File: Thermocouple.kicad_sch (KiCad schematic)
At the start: 9 parts, among them J7 K-TYPE THERMOCOUPLE, U11 MAX31856

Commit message: 9/13/2026 schematic work
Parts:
- C16, C17, C18: value 0.1uF -> 0.1u
- C19, C28: value 0.01uF -> 0.01u
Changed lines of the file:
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@@
 		(dnp no)
 		(property "Reference" "C18"
-			(at 142.748 77.216 0)
-			(show_name no)
-			(do_not_autoplace no)
-			(effects
-				(font
-					(size 1.27 1.27)
-				)
-				(justify left)
-			)
-		)
-		(property "Value" "0.1uF"
-			(at 147.066 77.47 0)
+			(at 146.558 71.628 90)
+			(show_name no)
+			(do_not_autoplace no)
+			(effects
+				(font
+					(size 1.27 1.27)
+				)
+				(justify left)
+			)
+		)
+		(property "Value" "0.1u"
+			(at 146.812 73.66 90)
 			(show_name no)
 			(do_not_autoplace no)
@@
 		(in_pos_files yes)
 		(dnp no)
-		(fields_autoplaced yes)
 		(property "Reference" "U11"
-			(at 169.7833 71.12 0)
+			(at 171.196 74.93 0)
 			(show_name no)
 			(do_not_autoplace no)
@@
 		)
 		(property "Value" "MAX31856"
-			(at 169.7833 73.66 0)
+			(at 168.656 102.87 0)
 			(show_name no)
 			(do_not_autoplace no)
@@
 			)
 		)
-		(property "Value" "0.1uF"
+		(property "Value" "0.1u"
 			(at 168.402 68.326 0)
 			(show_name no)
@@
 			)
 		)
-		(property "Value" "0.1uF"
+		(property "Value" "0.1u"
 			(at 156.21 68.326 0)
 			(show_name no)
@@
 			)
 		)
-		(property "Value" "0.01uF"
-			(at 127 98.806 0)
+		(property "Value" "0.01u"
+			(at 127.508 98.806 0)
 			(show_name no)
 			(do_not_autoplace no)
@@
 			)
 		)
-		(property "Value" "0.01uF"
-			(at 135.89 98.806 0)
-			(show_name no)
-			(do_not_autoplace no)
+		(property "Value" "0.01u"
+			(at 136.652 98.806 0)
+			(show_name no)
+			(do_not_autoplace no)

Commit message: changed sheet names
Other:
- title: Thermocouple Input -> Thermocouple
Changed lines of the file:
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@@
 	(paper "A")
 	(title_block
-		(title "Thermocouple Input")
+		(title "Thermocouple")
 		(date "2026-09-08")
 		(rev "1")

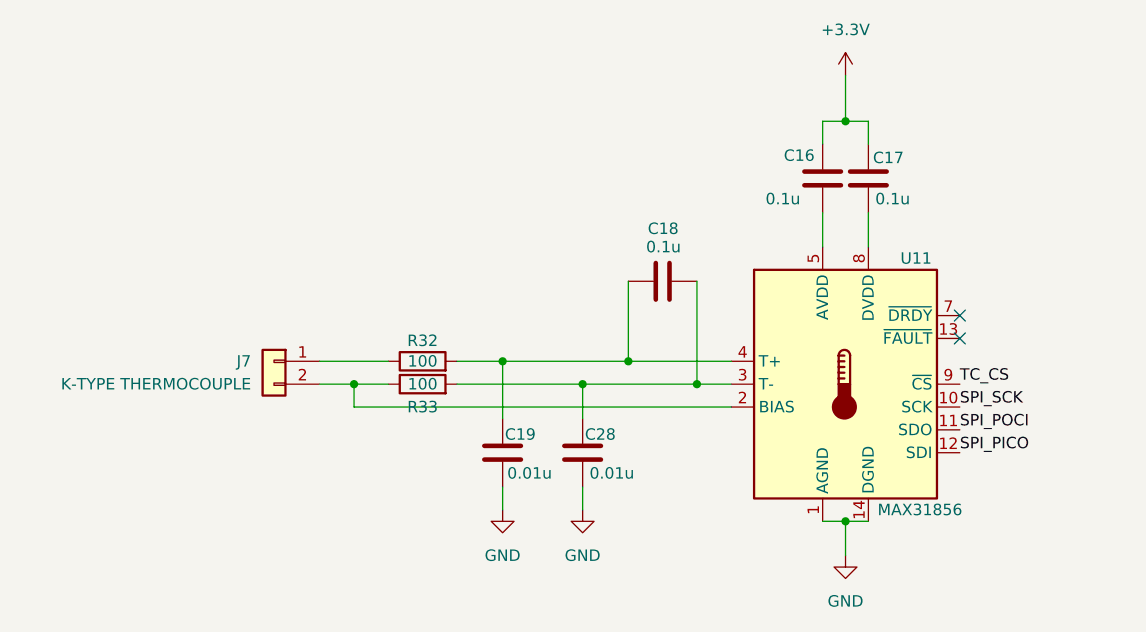
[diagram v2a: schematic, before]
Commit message: changed net labels to global labels
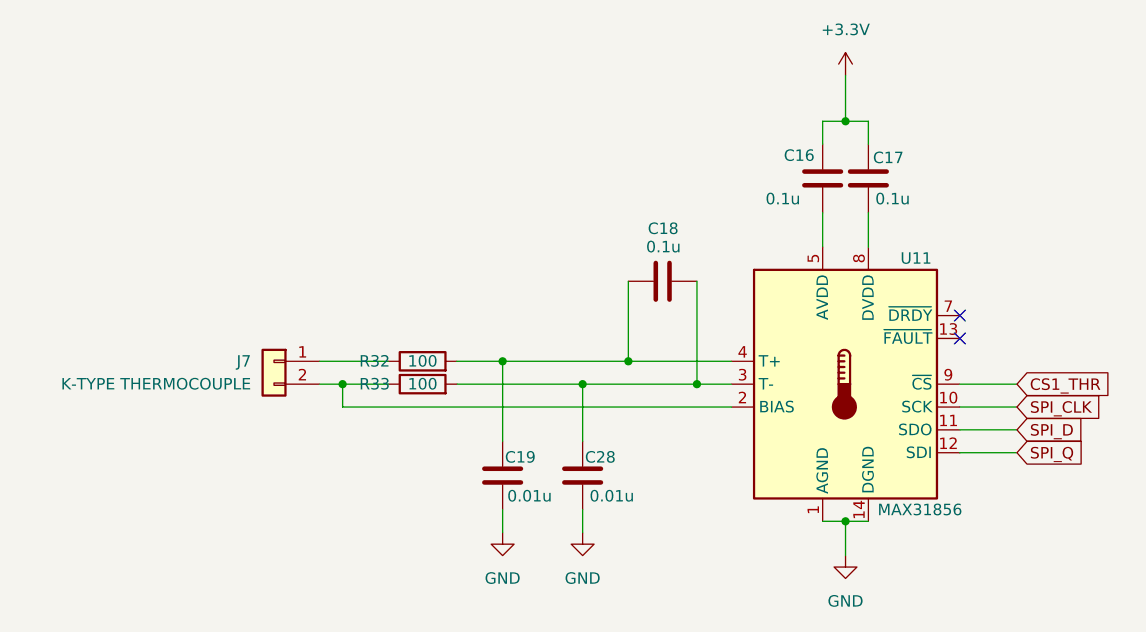
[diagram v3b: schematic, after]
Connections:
- net SPI_PICO renamed SPI_Q
- net SPI_POCI renamed SPI_D
- net SPI_SCK renamed SPI_CLK
- net TC_CS renamed CS1_THR
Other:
- moved on the sheet: C19, C28
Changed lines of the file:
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@@
 	)
 	(junction
-		(at 110.49 88.9)
+		(at 109.22 88.9)
 		(diameter 0)
 		(color 0 0 0 0)
@@
 	(wire
 		(pts
-			(xy 135.89 88.9) (xy 135.89 92.71)
+			(xy 135.89 88.9) (xy 135.89 95.25)
 		)
 		(stroke
@@
 	(wire
 		(pts
+			(xy 184.15 88.9) (xy 177.8 88.9)
+		)
+		(stroke
+			(width 0)
+			(type default)
+		)
+	)
+	(wire
+		(pts
+			(xy 184.15 91.44) (xy 177.8 91.44)
+		)
+		(stroke
+			(width 0)
+			(type default)
+		)
+	)
+	(wire
+		(pts
 			(xy 165.1 59.69) (xy 167.64 59.69)
 		)
@@
 	(wire
 		(pts
-			(xy 106.68 88.9) (xy 110.49 88.9)
-		)
-		(stroke
-			(width 0)
-			(type default)
-		)
-	)
-	(wire
-		(pts
-			(xy 127 86.36) (xy 127 92.71)
+			(xy 106.68 88.9) (xy 114.3 88.9)
+		)
+		(stroke
+			(width 0)
+			(type default)
+		)
+	)
+	(wire
+		(pts
+			(xy 127 86.36) (xy 127 95.25)
 		)
 		(stroke
@@
 	(wire
 		(pts
+			(xy 184.15 96.52) (xy 177.8 96.52)
+		)
+		(stroke
+			(width 0)
+			(type default)
+		)
+	)
+	(wire
+		(pts
+			(xy 184.15 93.98) (xy 177.8 93.98)
+		)
+		(stroke
+			(width 0)
+			(type default)
+		)
+	)
+	(wire
+		(pts
 			(xy 127 86.36) (xy 152.4 86.36)
 		)
@@
 	(wire
 		(pts
-			(xy 135.89 100.33) (xy 135.89 102.87)
+			(xy 135.89 102.87) (xy 135.89 105.41)
 		)
 		(stroke
@@
 	(wire
 		(pts
-			(xy 110.49 88.9) (xy 114.3 88.9)
-		)
-		(stroke
-			(width 0)
-			(type default)
-		)
-	)
-	(wire
-		(pts
-			(xy 127 100.33) (xy 127 102.87)
+			(xy 127 102.87) (xy 127 105.41)
 		)
 		(stroke
@@
 	(wire
 		(pts
-			(xy 110.49 91.44) (xy 110.49 88.9)
+			(xy 109.22 91.44) (xy 109.22 88.9)
 		)
 		(stroke
@@
 	(wire
 		(pts
-			(xy 152.4 91.44) (xy 110.49 91.44)
-		)
-		(stroke
-			(width 0)
-			(type default)
-		)
-	)
-	(label "SPI_PICO"
-		(at 177.8 96.52 0)
+			(xy 152.4 91.44) (xy 109.22 91.44)
+		)
+		(stroke
+			(width 0)
+			(type default)
+		)
+	)
+	(global_label "SPI_Q"
+		(shape input)
+		(at 184.15 96.52 0)
+		(fields_autoplaced yes)
 		(effects
 			(font
 				(size 1.27 1.27)
 			)
-			(justify left bottom)
-		)
-	)
-	(label "SPI_SCK"
-		(at 177.8 91.44 0)
+			(justify left)
+		)
+		(property "Intersheetrefs" "${INTERSHEET_REFS}"
+			(at 192.5176 96.52 0)
+			(hide yes)
+			(show_name no)
+			(do_not_autoplace no)
+			(effects
+				(font
+					(size 1.27 1.27)
+				)
+				(justify left)
+			)
+		)
+	)
+	(global_label "SPI_D"
+		(shape input)
+		(at 184.15 93.98 0)
+		(fields_autoplaced yes)
 		(effects
 			(font
 				(size 1.27 1.27)
 			)
-			(justify left bottom)
-		)
-	)
-	(label "SPI_POCI"
-		(at 177.8 93.98 0)
+			(justify left)
+		)
+		(property "Intersheetrefs" "${INTERSHEET_REFS}"
+			(at 192.4571 93.98 0)
+			(hide yes)
+			(show_name no)
+			(do_not_autoplace no)
+			(effects
+				(font
+					(size 1.27 1.27)
+				)
+				(justify left)
+			)
+		)
+	)
+	(global_label "SPI_CLK"
+		(shape input)
+		(at 184.15 91.44 0)
+		(fields_autoplaced yes)
 		(effects
 			(font
 				(size 1.27 1.27)
 			)
-			(justify left bottom)
-		)
-	)
-	(label "TC_CS"
-		(at 177.8 88.9 0)
+			(justify left)
+		)
+		(property "Intersheetrefs" "${INTERSHEET_REFS}"
+			(at 194.7552 91.44 0)
+			(hide yes)
+			(show_name no)
+			(do_not_autoplace no)
+			(effects
+				(font
+					(size 1.27 1.27)
+				)
+				(justify left)
+			)
+		)
+	)
+	(global_label "CS1_THR"
+		(shape input)
+		(at 184.15 88.9 0)
+		(fields_autoplaced yes)
 		(effects
 			(font
 				(size 1.27 1.27)
 			)
-			(justify left bottom)
+			(justify left)
+		)
+		(property "Intersheetrefs" "${INTERSHEET_REFS}"
+			(at 195.3599 88.9 0)
+			(hide yes)
+			(show_name no)
+			(do_not_autoplace no)
+			(effects
+				(font
+					(size 1.27 1.27)
+				)
+				(justify left)
+			)
 		)
 	)
@@
 	(symbol
 		(lib_id "power:GND")
-		(at 135.89 102.87 0)
+		(at 135.89 105.41 0)
 		(unit 1)
 		(body_style 1)
@@
 		(fields_autoplaced yes)
 		(property "Reference" "#PWR058"
-			(at 135.89 109.22 0)
+			(at 135.89 111.76 0)
 			(hide yes)
 			(show_name no)
@@
 		)
 		(property "Value" "GND"
-			(at 135.89 107.95 0)
+			(at 135.89 110.49 0)
 			(show_name no)
 			(do_not_autoplace no)
@@
 		)
 		(property "Footprint" ""
-			(at 135.89 102.87 0)
+			(at 135.89 105.41 0)
 			(hide yes)
 			(show_name no)
@@
 		)
 		(property "Datasheet" ""
-			(at 135.89 102.87 0)
+			(at 135.89 105.41 0)
 			(hide yes)
 			(show_name no)
@@
 		)
 		(property "Description" "Power symbol creates a global label with name \"GND\" , ground"
-			(at 135.89 102.87 0)
+			(at 135.89 105.41 0)
 			(hide yes)
 			(show_name no)
@@
 		(dnp no)
 		(property "Reference" "R32"
-			(at 118.11 84.074 90)
+			(at 112.776 86.36 90)
 			(show_name no)
 			(do_not_autoplace no)
@@
 		(dnp no)
 		(property "Reference" "R33"
-			(at 118.11 91.44 90)
+			(at 112.776 88.9 90)
 			(show_name no)
 			(do_not_autoplace no)
@@
 	(symbol
 		(lib_id "power:GND")
-		(at 127 102.87 0)
+		(at 127 105.41 0)
 		(unit 1)
 		(body_style 1)
@@
 		(fields_autoplaced yes)
 		(property "Reference" "#PWR057"
-			(at 127 109.22 0)
+			(at 127 111.76 0)
 			(hide yes)
 			(show_name no)
@@
 		)
 		(property "Value" "GND"
-			(at 127 107.95 0)
+			(at 127 110.49 0)
 			(show_name no)
 			(do_not_autoplace no)
@@
 		)
 		(property "Footprint" ""
-			(at 127 102.87 0)
+			(at 127 105.41 0)
 			(hide yes)
 			(show_name no)
@@
 		)
 		(property "Datasheet" ""
-			(at 127 102.87 0)
+			(at 127 105.41 0)
 			(hide yes)
 			(show_name no)
@@
 		)
 		(property "Description" "Power symbol creates a global label with name \"GND\" , ground"
-			(at 127 102.87 0)
+			(at 127 105.41 0)
 			(hide yes)
 			(show_name no)
@@
 	(symbol
 		(lib_id "Device:C")
-		(at 127 96.52 0)
+		(at 127 99.06 0)
 		(unit 1)
 		(body_style 1)
@@
 		(dnp no)
 		(property "Reference" "C19"
-			(at 127.254 94.488 0)
+			(at 127.254 97.028 0)
 			(show_name no)
 			(do_not_autoplace no)
@@
 		)
 		(property "Value" "0.01u"
-			(at 127.508 98.806 0)
+			(at 127.508 101.346 0)
 			(show_name no)
 			(do_not_autoplace no)
@@
 		)
 		(property "Footprint" "Package_SO:TSSOP-14_4.4x5mm_P0.65mm"
-			(at 127.9652 100.33 0)
+			(at 127.9652 102.87 0)
 			(hide yes)
 			(show_name no)
@@
 		)
 		(property "Datasheet" ""
-			(at 127 96.52 0)
+			(at 127 99.06 0)
 			(hide yes)
 			(show_name no)
@@
 		)
 		(property "Description" "Unpolarized capacitor"
-			(at 127 96.52 0)
+			(at 127 99.06 0)
 			(hide yes)
 			(show_name no)
@@
 	(symbol
 		(lib_id "Device:C")
-		(at 135.89 96.52 0)
+		(at 135.89 99.06 0)
 		(unit 1)
 		(body_style 1)
@@
 		(dnp no)
 		(property "Reference" "C28"
-			(at 136.144 94.488 0)
+			(at 136.144 97.028 0)
 			(show_name no)
 			(do_not_autoplace no)
@@
 		)
 		(property "Value" "0.01u"
-			(at 136.652 98.806 0)
+			(at 136.652 101.346 0)
 			(show_name no)
 			(do_not_autoplace no)
@@
 		)
 		(property "Footprint" "Package_SO:TSSOP-14_4.4x5mm_P0.65mm"
-			(at 136.8552 100.33 0)
+			(at 136.8552 102.87 0)
 			(hide yes)
 			(show_name no)
@@
 		)
 		(property "Datasheet" ""
-			(at 135.89 96.52 0)
+			(at 135.89 99.06 0)
 			(hide yes)
 			(show_name no)
@@
 		)
 		(property "Description" "Unpolarized capacitor"
-			(at 135.89 96.52 0)
-			(hide yes)
-			(show_name no)
+			(at 135.89 99.06 0)
+			(hide yes)
+			(show_name no)

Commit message: added gnd to inputs
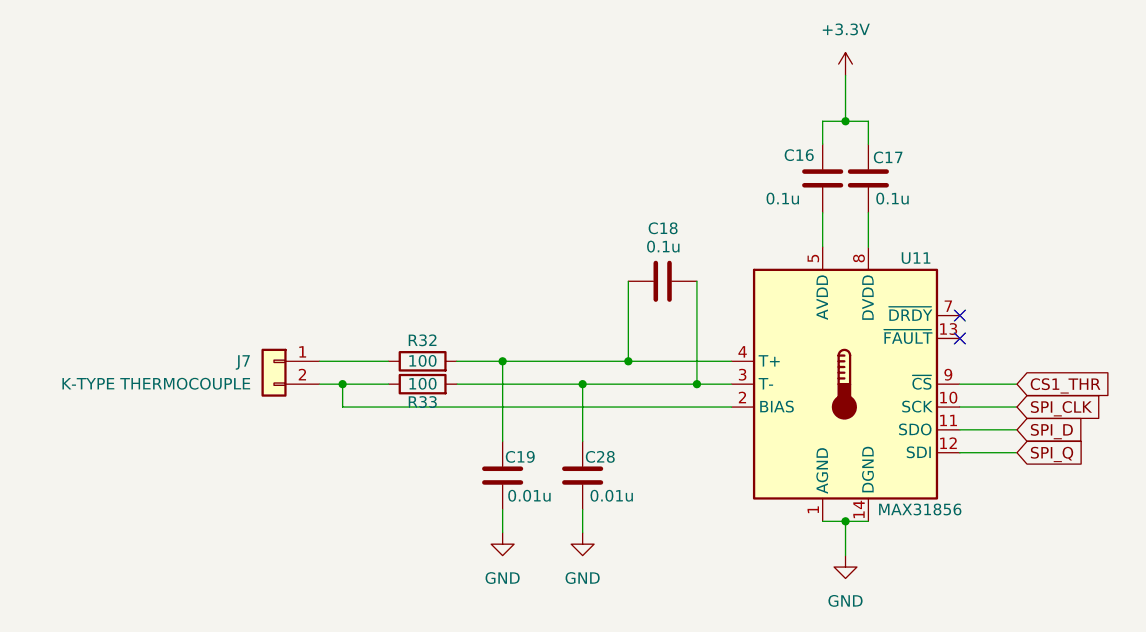
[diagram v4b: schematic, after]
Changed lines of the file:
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@@
 		(dnp no)
 		(property "Reference" "R32"
-			(at 112.776 86.36 90)
+			(at 118.11 84.074 90)
 			(show_name no)
 			(do_not_autoplace no)
@@
 		(dnp no)
 		(property "Reference" "R33"
-			(at 112.776 88.9 90)
+			(at 118.11 90.932 90)
 			(show_name no)
 			(do_not_autoplace no)

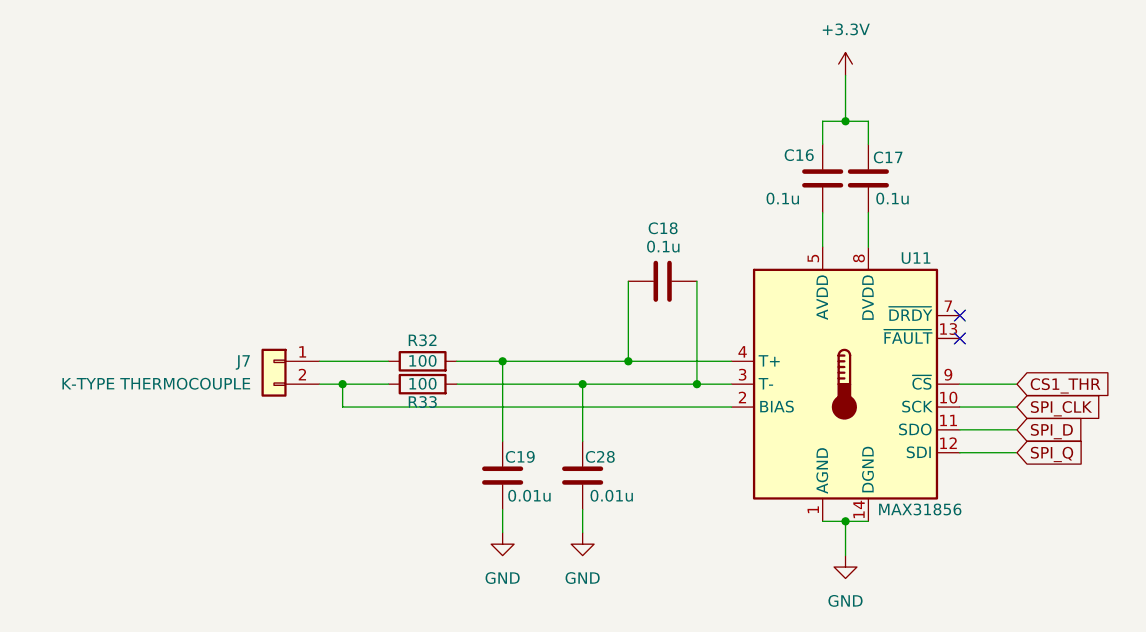
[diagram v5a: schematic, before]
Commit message: removed grounds from inputs
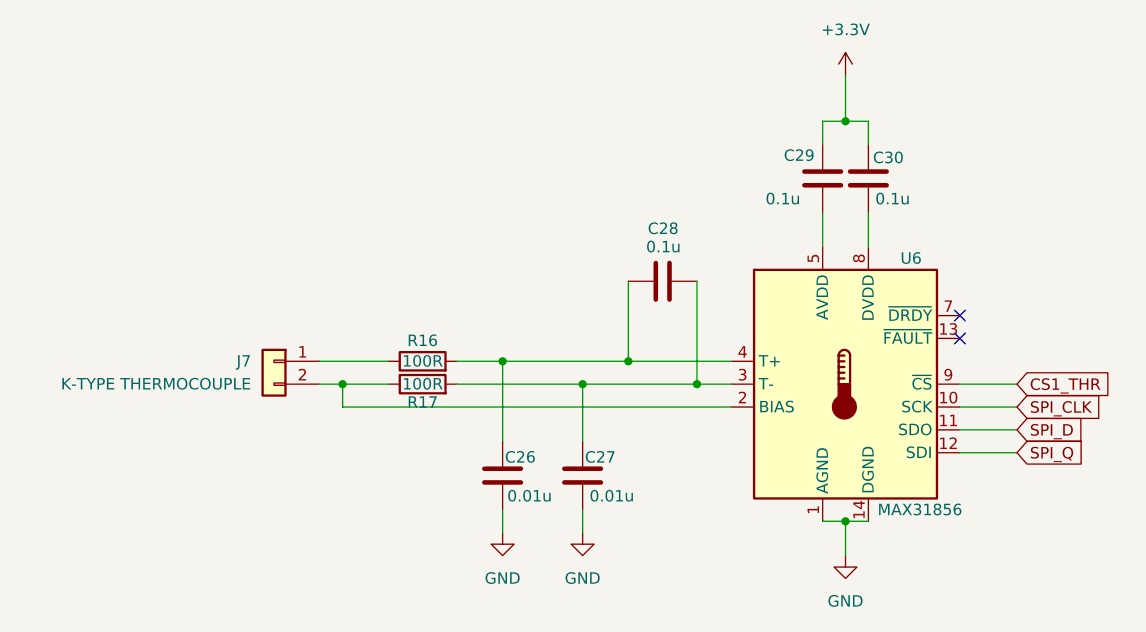
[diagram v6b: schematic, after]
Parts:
- R16: renamed from R32; value 100 -> 100R
- R17: renamed from R33; value 100 -> 100R
- renumbered C19 to C26, C28 to C27, C18 to C28, C16 to C29, C17 to C30, U11 to U6
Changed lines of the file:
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@@
 		(in_pos_files yes)
 		(dnp no)
-		(property "Reference" "C18"
+		(property "Reference" "C28"
 			(at 146.558 71.628 90)
 			(show_name no)
@@
 			(project "slapdaq-board"
 				(path "/13b31ec5-9d44-45c3-b3e5-a18c48e5f516/eb21b777-61c4-4e0c-995e-92861c8d5ad5"
-					(reference "C18")
+					(reference "C28")
 					(unit 1)
 				)
@@
 		(in_pos_files yes)
 		(dnp no)
-		(property "Reference" "U11"
+		(property "Reference" "U6"
 			(at 171.196 74.93 0)
 			(show_name no)
@@
 			(project "slapdaq-board"
 				(path "/13b31ec5-9d44-45c3-b3e5-a18c48e5f516/eb21b777-61c4-4e0c-995e-92861c8d5ad5"
-					(reference "U11")
+					(reference "U6")
 					(unit 1)
 				)
@@
 		(dnp no)
 		(fields_autoplaced yes)
-		(property "Reference" "#PWR058"
+		(property "Reference" "#PWR050"
 			(at 135.89 111.76 0)
 			(hide yes)
@@
 			(project "slapdaq-board"
 				(path "/13b31ec5-9d44-45c3-b3e5-a18c48e5f516/eb21b777-61c4-4e0c-995e-92861c8d5ad5"
-					(reference "#PWR058")
+					(reference "#PWR050")
 					(unit 1)
 				)
@@
 		(in_pos_files yes)
 		(dnp no)
-		(property "Reference" "R32"
+		(property "Reference" "R16"
 			(at 118.11 84.074 90)
 			(show_name no)
@@
 			)
 		)
-		(property "Value" "100"
+		(property "Value" "100R"
 			(at 118.11 86.36 90)
 			(show_name no)
@@
 			(project "slapdaq-board"
 				(path "/13b31ec5-9d44-45c3-b3e5-a18c48e5f516/eb21b777-61c4-4e0c-995e-92861c8d5ad5"
-					(reference "R32")
+					(reference "R16")
 					(unit 1)
 				)
@@
 		(in_pos_files yes)
 		(dnp no)
-		(property "Reference" "R33"
+		(property "Reference" "R17"
 			(at 118.11 90.932 90)
 			(show_name no)
@@
 			)
 		)
-		(property "Value" "100"
+		(property "Value" "100R"
 			(at 118.11 88.9 90)
 			(show_name no)
@@
 			(project "slapdaq-board"
 				(path "/13b31ec5-9d44-45c3-b3e5-a18c48e5f516/eb21b777-61c4-4e0c-995e-92861c8d5ad5"
-					(reference "R33")
+					(reference "R17")
 					(unit 1)
 				)
@@
 		(dnp no)
 		(fields_autoplaced yes)
-		(property "Reference" "#PWR057"
+		(property "Reference" "#PWR049"
 			(at 127 111.76 0)
 			(hide yes)
@@
 			(project "slapdaq-board"
 				(path "/13b31ec5-9d44-45c3-b3e5-a18c48e5f516/eb21b777-61c4-4e0c-995e-92861c8d5ad5"
-					(reference "#PWR057")
+					(reference "#PWR049")
 					(unit 1)
 				)
@@
 		(in_pos_files yes)
 		(dnp no)
-		(property "Reference" "C17"
+		(property "Reference" "C30"
 			(at 168.148 63.754 0)
 			(show_name no)
@@
 			(project "slapdaq-board"
 				(path "/13b31ec5-9d44-45c3-b3e5-a18c48e5f516/eb21b777-61c4-4e0c-995e-92861c8d5ad5"
-					(reference "C17")
+					(reference "C30")
 					(unit 1)
 				)
@@
 		(in_pos_files yes)
 		(dnp no)
-		(property "Reference" "C16"
+		(property "Reference" "C29"
 			(at 158.242 63.5 0)
 			(show_name no)
@@
 			(project "slapdaq-board"
 				(path "/13b31ec5-9d44-45c3-b3e5-a18c48e5f516/eb21b777-61c4-4e0c-995e-92861c8d5ad5"
-					(reference "C16")
+					(reference "C29")
 					(unit 1)
 				)
@@
 		(dnp no)
 		(fields_autoplaced yes)
-		(property "Reference" "#PWR039"
+		(property "Reference" "#PWR052"
 			(at 165.1 114.3 0)
 			(hide yes)
@@
 			(project "slapdaq-board"
 				(path "/13b31ec5-9d44-45c3-b3e5-a18c48e5f516/eb21b777-61c4-4e0c-995e-92861c8d5ad5"
-					(reference "#PWR039")
+					(reference "#PWR052")
 					(unit 1)
 				)
@@
 		(in_pos_files yes)
 		(dnp no)
-		(property "Reference" "C19"
+		(property "Reference" "C26"
 			(at 127.254 97.028 0)
 			(show_name no)
@@
 			(project "slapdaq-board"
 				(path "/13b31ec5-9d44-45c3-b3e5-a18c48e5f516/eb21b777-61c4-4e0c-995e-92861c8d5ad5"
-					(reference "C19")
+					(reference "C26")
 					(unit 1)
 				)
@@
 		(in_pos_files yes)
 		(dnp no)
-		(property "Reference" "C28"
+		(property "Reference" "C27"
 			(at 136.144 97.028 0)
 			(show_name no)
@@
 			(project "slapdaq-board"
 				(path "/13b31ec5-9d44-45c3-b3e5-a18c48e5f516/eb21b777-61c4-4e0c-995e-92861c8d5ad5"
-					(reference "C28")
+					(reference "C27")
 					(unit 1)
 				)
@@
 		(dnp no)
 		(fields_autoplaced yes)
-		(property "Reference" "#PWR056"
+		(property "Reference" "#PWR051"
 			(at 165.1 58.42 0)
 			(hide yes)
@@
 			(project "slapdaq-board"
 				(path "/13b31ec5-9d44-45c3-b3e5-a18c48e5f516/eb21b777-61c4-4e0c-995e-92861c8d5ad5"
-					(reference "#PWR056")
-					(unit 1)
-				)
+					(reference "#PWR051")
+					(unit 1)
+				)

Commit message: 9/20/2026 schematic work
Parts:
- C26, C27: footprint Package_SO:TSSOP-14_4.4x5mm_P0.65mm -> Capacitor_SMD:C_1206_3216Metric_Pad1.33x1.80mm_HandSolder; MPN (none) -> GRM31CR73A103KW03L; Mouser Link (none) -> https://www.mouser.com/en/ProductDetail/Murata-Electronics/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
- C28, C29, C30: footprint Package_SO:TSSOP-14_4.4x5mm_P0.65mm -> Capacitor_SMD:C_1206_3216Metric_Pad1.33x1.80mm_HandSolder; MPN (none) -> GRM31CR72E104KW03L; Mouser Link (none) -> https://www.mouser.com/en/ProductDetail/Murata-Electronics/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
- J7: footprint TerminalBlock_Phoenix:TerminalBlock_Phoenix_MKDS-1,5-2-5.08_1x02_P5.08mm_Horizontal -> (none); MPN 1715721 -> (none)
- R18: renamed from R16; footprint (none) -> Resistor_SMD:R_1206_3216Metric_Pad1.30x1.75mm_HandSolder; MPN (none) -> RC1206DR-07100RL; Mouser Link (none) -> https://www.mouser.com/en/ProductDetail/YAGEO/RC1206DR-0710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
- R19: renamed from R17; footprint (none) -> Resistor_SMD:R_1206_3216Metric_Pad1.30x1.75mm_HandSolder; MPN (none) -> RC1206DR-07100RL; Mouser Link (none) -> https://www.mouser.com/en/ProductDetail/YAGEO/RC1206DR-0710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
- U7: renamed from U6; Mouser Link (none) -> https://www.mouser.com/en/ProductDetail/Analog-Devices-Maxi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
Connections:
- net +3.3V: now also U7.5 (AVDD), U7.8 (DVDD)
- net GND: now also C29.2, C30.2
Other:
- company: Slap DAQ -> Faster Than Sound
- title: Thermocouple -> SlapDAQ - Thermocouple
- moved on the sheet: C29, C30
